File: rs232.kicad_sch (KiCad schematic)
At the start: 7 parts, among them J7 RS232_0, J8 RS232_1, U2 MAX232

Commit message: Export common fields to all sheets
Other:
- company: (none) -> TXnology
- title: (none) -> USB-to-quad UART
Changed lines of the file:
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@@
 	(paper "A4")
 	(title_block
+		(title "USB-to-quad UART")
+		(date "2024-08-30")
 		(rev "rev. 2")
+		(company "TXnology")
+		(comment 1 "Engineer: Bence Csókás")
 	)
 	(wire

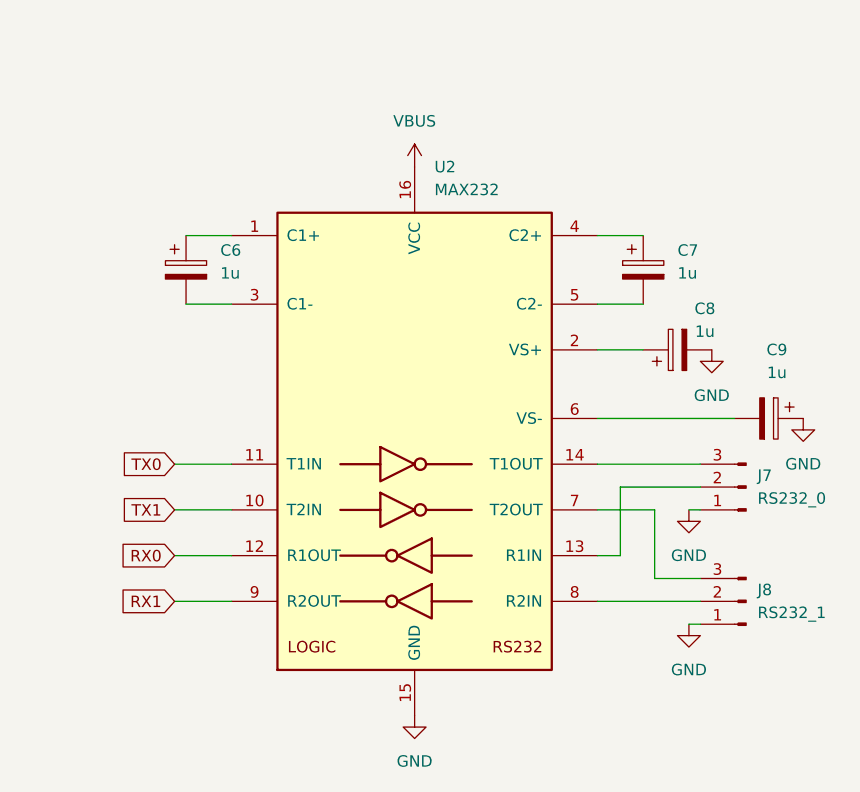
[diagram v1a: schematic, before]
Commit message: Add option for ADM202
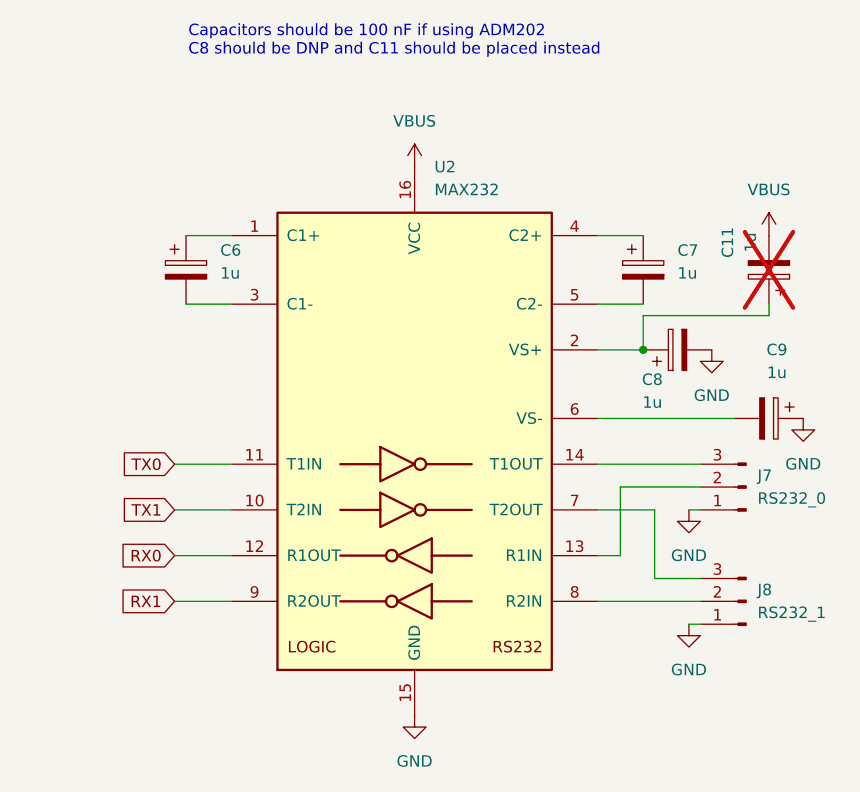
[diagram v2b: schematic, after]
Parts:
- added C11: 1u, Capacitor_SMD:C_0603_1608Metric, symbol Device:C_Polarized
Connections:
- net VBUS: now also C11.2
- net at C8.1, U2.2 (VS+): now also C11.1
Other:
- note added: "Capacitors should be 100 nF if using ADM202 C8 should be DNP and C11 should be placed instead"
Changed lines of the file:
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@@
 		(comment 1 "Engineer: Bence Csókás")
 	)
+	(junction
+		(at 247.65 73.66)
+		(diameter 0)
+		(color 0 0 0 0)
+	)
 	(wire
 		(pts
@@
 	(wire
 		(pts
+			(xy 261.62 68.58) (xy 261.62 69.85)
+		)
+		(stroke
+			(width 0)
+			(type default)
+		)
+	)
+	(wire
+		(pts
 			(xy 245.11 88.9) (xy 254 88.9)
 		)
@@
 	(wire
 		(pts
+			(xy 247.65 69.85) (xy 247.65 73.66)
+		)
+		(stroke
+			(width 0)
+			(type default)
+		)
+	)
+	(wire
+		(pts
 			(xy 195.58 101.6) (xy 201.93 101.6)
 		)
@@
 	(wire
 		(pts
+			(xy 261.62 69.85) (xy 247.65 69.85)
+		)
+		(stroke
+			(width 0)
+			(type default)
+		)
+	)
+	(wire
+		(pts
 			(xy 252.73 91.44) (xy 254 91.44)
 		)
@@
 			(width 0)
 			(type default)
+		)
+	)
+	(text "Capacitors should be 100 nF if using ADM202\nC8 should be DNP and C11 should be placed instead"
+		(exclude_from_sim no)
+		(at 197.104 39.37 0)
+		(effects
+			(font
+				(size 1.27 1.27)
+			)
+			(justify left)
 		)
 	)
@@
 	)
 	(symbol
+		(lib_id "power:VBUS")
+		(at 261.62 60.96 0)
+		(unit 1)
+		(exclude_from_sim no)
+		(in_bom yes)
+		(on_board yes)
+		(dnp no)
+		(fields_autoplaced yes)
+		(property "Reference" "#PWR056"
+			(at 261.62 64.77 0)
+			(effects
+				(font
+					(size 1.27 1.27)
+				)
+				(hide yes)
+			)
+		)
+		(property "Value" "VBUS"
+			(at 261.62 55.88 0)
+			(effects
+				(font
+					(size 1.27 1.27)
+				)
+			)
+		)
+		(property "Footprint" ""
+			(at 261.62 60.96 0)
+			(effects
+				(font
+					(size 1.27 1.27)
+				)
+				(hide yes)
+			)
+		)
+		(property "Datasheet" ""
+			(at 261.62 60.96 0)
+			(effects
+				(font
+					(size 1.27 1.27)
+				)
+				(hide yes)
+			)
+		)
+		(property "Description" "Power symbol creates a global label with name \"VBUS\""
+			(at 261.62 60.96 0)
+			(effects
+				(font
+					(size 1.27 1.27)
+				)
+				(hide yes)
+			)
+		)
+		(pin "1"
+		)
+		(instances
+			(project "CR-serial"
+				(path "/9106c304-8c09-42ff-a431-8edd4bec763c/b52b5eef-cacd-4097-a1da-57bb1cf9d067"
+					(reference "#PWR056")
+					(unit 1)
+				)
+			)
+		)
+	)
+	(symbol
 		(lib_id "Connector:Conn_01x03_Pin")
 		(at 259.08 88.9 180)
@@
 	(symbol
 		(lib_id "Device:C_Polarized")
+		(at 261.62 64.77 180)
+		(unit 1)
+		(exclude_from_sim no)
+		(in_bom yes)
+		(on_board yes)
+		(dnp yes)
+		(property "Reference" "C11"
+			(at 257.048 61.722 90)
+			(effects
+				(font
+					(size 1.27 1.27)
+				)
+			)
+		)
+		(property "Value" "1u"
+			(at 259.588 61.722 90)
+			(effects
+				(font
+					(size 1.27 1.27)
+				)
+			)
+		)
+		(property "Footprint" "Capacitor_SMD:C_0603_1608Metric"
+			(at 260.6548 60.96 0)
+			(effects
+				(font
+					(size 1.27 1.27)
+				)
+				(hide yes)
+			)
+		)
+		(property "Datasheet" "~"
+			(at 261.62 64.77 0)
+			(effects
+				(font
+					(size 1.27 1.27)
+				)
+				(hide yes)
+			)
+		)
+		(property "Description" "Polarized capacitor"
+			(at 261.62 64.77 0)
+			(effects
+				(font
+					(size 1.27 1.27)
+				)
+				(hide yes)
+			)
+		)
+		(pin "2"
+		)
+		(pin "1"
+		)
+		(instances
+			(project "CR-serial"
+				(path "/9106c304-8c09-42ff-a431-8edd4bec763c/b52b5eef-cacd-4097-a1da-57bb1cf9d067"
+					(reference "C11")
+					(unit 1)
+				)
+			)
+		)
+	)
+	(symbol
+		(lib_id "Device:C_Polarized")
 		(at 261.62 81.28 270)
 		(unit 1)
@@
 		(dnp no)
 		(property "Reference" "C8"
-			(at 254.508 69.088 90)
+			(at 248.666 76.962 90)
 			(effects
 				(font
@@
 		)
 		(property "Value" "1u"
-			(at 254.508 71.628 90)
-			(effects
-				(font
+			(at 248.666 79.502 90)
+			(effects
+				(font

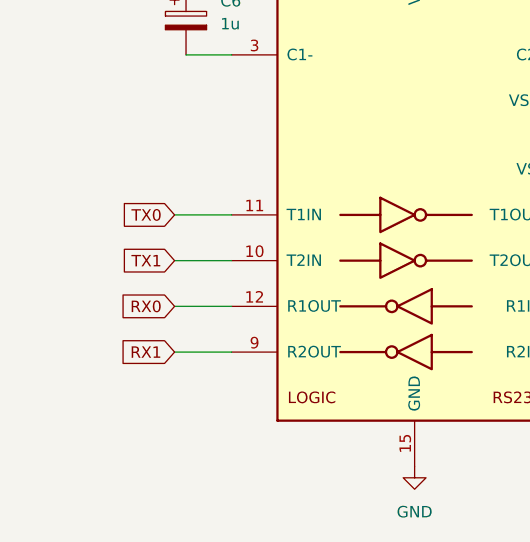
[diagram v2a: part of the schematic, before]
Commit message: Add RS232 RX enable for more flexibility
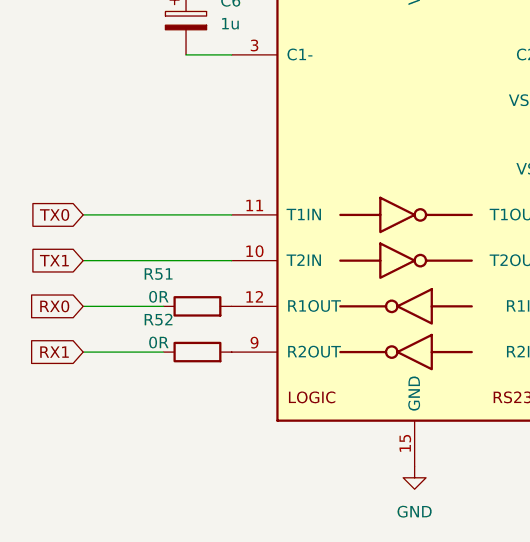
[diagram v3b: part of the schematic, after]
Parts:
- added R51, R52: 0R, Resistor_SMD:R_0603_1608Metric, symbol Device:R
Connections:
- net RX0: now also R51.1; no longer U2.12 (R1OUT)
- net RX1: now also R52.1; no longer U2.9 (R2OUT)
- new net: R51.2, U2.12 (R1OUT)
- new net: R52.2, U2.9 (R2OUT)
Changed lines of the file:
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@@
 		(title "USB-to-quad UART")
 		(date "2024-08-30")
-		(rev "rev. 2")
+		(rev "rev. 3")
 		(company "TXnology")
 		(comment 1 "Engineer: Bence Csókás")
@@
 	(wire
 		(pts
-			(xy 195.58 86.36) (xy 201.93 86.36)
+			(xy 185.42 86.36) (xy 201.93 86.36)
 		)
 		(stroke
@@
 	(wire
 		(pts
-			(xy 195.58 101.6) (xy 201.93 101.6)
+			(xy 185.42 101.6) (xy 194.31 101.6)
 		)
 		(stroke
@@
 	(wire
 		(pts
-			(xy 195.58 96.52) (xy 201.93 96.52)
+			(xy 185.42 96.52) (xy 194.31 96.52)
 		)
 		(stroke
@@
 	(wire
 		(pts
-			(xy 195.58 91.44) (xy 201.93 91.44)
+			(xy 185.42 91.44) (xy 201.93 91.44)
 		)
 		(stroke
@@
 	(global_label "RX0"
 		(shape input)
-		(at 195.58 96.52 180)
+		(at 185.42 96.52 180)
 		(fields_autoplaced yes)
 		(effects
@@
 		)
 		(property "Intersheetrefs" "${INTERSHEET_REFS}"
-			(at 188.9058 96.52 0)
+			(at 178.7458 96.52 0)
 			(effects
 				(font
@@
 	(global_label "TX1"
 		(shape input)
-		(at 195.58 91.44 180)
+		(at 185.42 91.44 180)
 		(fields_autoplaced yes)
 		(effects
@@
 		)
 		(property "Intersheetrefs" "${INTERSHEET_REFS}"
-			(at 189.2082 91.44 0)
+			(at 179.0482 91.44 0)
 			(effects
 				(font
@@
 	(global_label "RX1"
 		(shape input)
-		(at 195.58 101.6 180)
+		(at 185.42 101.6 180)
 		(fields_autoplaced yes)
 		(effects
@@
 		)
 		(property "Intersheetrefs" "${INTERSHEET_REFS}"
-			(at 188.9058 101.6 0)
+			(at 178.7458 101.6 0)
 			(effects
 				(font
@@
 	(global_label "TX0"
 		(shape input)
-		(at 195.58 86.36 180)
+		(at 185.42 86.36 180)
 		(fields_autoplaced yes)
 		(effects
@@
 		)
 		(property "Intersheetrefs" "${INTERSHEET_REFS}"
-			(at 189.2082 86.36 0)
+			(at 179.0482 86.36 0)
 			(effects
 				(font
@@
 				(path "/9106c304-8c09-42ff-a431-8edd4bec763c/b52b5eef-cacd-4097-a1da-57bb1cf9d067"
 					(reference "J7")
+					(unit 1)
+				)
+			)
+		)
+	)
+	(symbol
+		(lib_id "Device:R")
+		(at 198.12 101.6 90)
+		(unit 1)
+		(exclude_from_sim no)
+		(in_bom yes)
+		(on_board yes)
+		(dnp no)
+		(property "Reference" "R52"
+			(at 193.802 98.044 90)
+			(effects
+				(font
+					(size 1.27 1.27)
+				)
+			)
+		)
+		(property "Value" "0R"
+			(at 193.802 100.584 90)
+			(effects
+				(font
+					(size 1.27 1.27)
+				)
+			)
+		)
+		(property "Footprint" "Resistor_SMD:R_0603_1608Metric"
+			(at 198.12 103.378 90)
+			(effects
+				(font
+					(size 1.27 1.27)
+				)
+				(hide yes)
+			)
+		)
+		(property "Datasheet" "~"
+			(at 198.12 101.6 0)
+			(effects
+				(font
+					(size 1.27 1.27)
+				)
+				(hide yes)
+			)
+		)
+		(property "Description" "Resistor"
+			(at 198.12 101.6 0)
+			(effects
+				(font
+					(size 1.27 1.27)
+				)
+				(hide yes)
+			)
+		)
+		(pin "2"
+		)
+		(pin "1"
+		)
+		(instances
+			(project "CR-serial"
+				(path "/9106c304-8c09-42ff-a431-8edd4bec763c/b52b5eef-cacd-4097-a1da-57bb1cf9d067"
+					(reference "R52")
 					(unit 1)
 				)
@@
 		(on_board yes)
 		(dnp no)
-		(fields_autoplaced yes)
 		(property "Reference" "#PWR028"
 			(at 222.25 57.15 0)
@@
 					(unit 1)
 				)
+			)
+		)
+	)
+	(symbol
+		(lib_id "Device:R")
+		(at 198.12 96.52 90)
+		(unit 1)
+		(exclude_from_sim no)
+		(in_bom yes)
+		(on_board yes)
+		(dnp no)
+		(property "Reference" "R51"
+			(at 193.802 92.964 90)
+			(effects
+				(font
+					(size 1.27 1.27)
+				)
+			)
+		)
+		(property "Value" "0R"
+			(at 193.802 95.504 90)
+			(effects
+				(font
+					(size 1.27 1.27)
+				)
+			)
+		)
+		(property "Footprint" "Resistor_SMD:R_0603_1608Metric"
+			(at 198.12 98.298 90)
+			(effects
+				(font
+					(size 1.27 1.27)
+				)
+				(hide yes)
+			)
+		)
+		(property "Datasheet" "~"
+			(at 198.12 96.52 0)
+			(effects
+				(font
+					(size 1.27 1.27)
+				)
+				(hide yes)
+			)
+		)
+		(property "Description" "Resistor"
+			(at 198.12 96.52 0)
+			(effects
+				(font
+					(size 1.27 1.27)
+				)
+				(hide yes)
+			)
+		)
+		(pin "2"
+		)
+		(pin "1"
+		)
+		(instances
+			(project ""
+				(path "/9106c304-8c09-42ff-a431-8edd4bec763c/b52b5eef-cacd-4097-a1da-57bb1cf9d067"
+					(reference "R51")
+					(unit 1)
+				)
